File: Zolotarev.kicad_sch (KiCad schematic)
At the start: 176 parts, among them J1 RF_IN, J2 RF_OUT, J3 Conn_02x05_Odd_Even, K1 G5LE-1, K10 G5LE-1, K11 G5LE-1, K12 G5LE-1, K13 G5LE-1, K14 G5LE-1, K2 G5LE-1, K3 G5LE-1, K4 G5LE-1, K5 G5LE-1, K6 G5LE-1, K7 G5LE-1, K8 G5LE-1, K9 G5LE-1

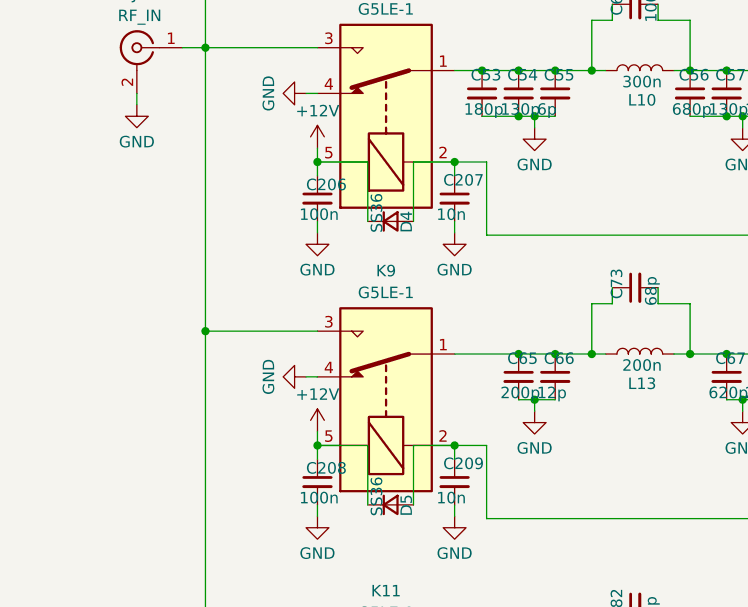
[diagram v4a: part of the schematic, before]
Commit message: 5 bands routed, 2 more to come
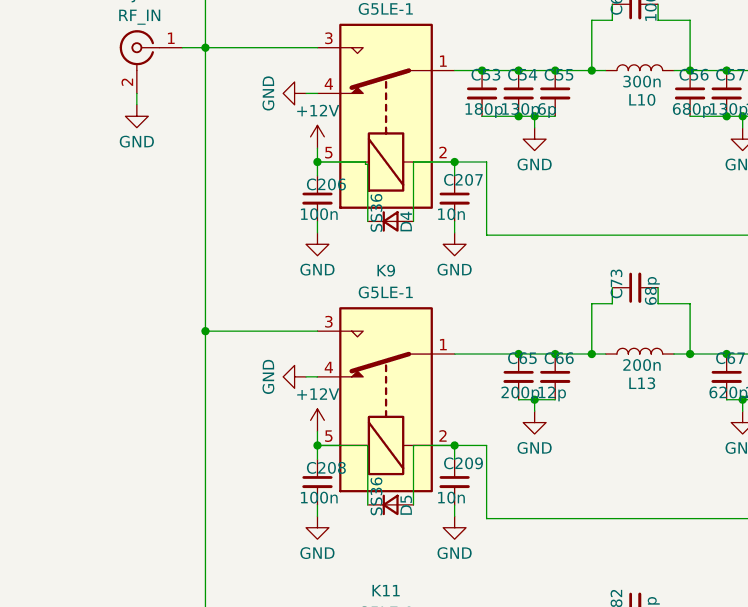
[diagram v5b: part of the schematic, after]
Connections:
- net +12V: now also D4.1 (K), D5.1 (K)
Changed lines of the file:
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@@
 	(wire
 		(pts
-			(xy 46.99 167.64) (xy 41.656 167.64)
+			(xy 46.99 167.64) (xy 41.402 167.64)
 		)
 		(stroke
@@
 	(wire
 		(pts
+			(xy 46.736 136.398) (xy 46.99 136.398)
+		)
+		(stroke
+			(width 0)
+			(type default)
+		)
+	)
+	(wire
+		(pts
 			(xy 110.744 62.992) (xy 112.522 62.992)
 		)
@@
 	(wire
 		(pts
-			(xy 46.99 136.144) (xy 41.656 136.144)
+			(xy 46.736 136.144) (xy 41.402 136.144)
 		)
 		(stroke
@@
 	(wire
 		(pts
-			(xy 46.99 142.748) (xy 46.99 136.144)
+			(xy 46.736 136.398) (xy 46.736 136.144)
 		)
 		(stroke
@@
 		)
 		(stroke
+			(width 0)
+			(type default)
+		)
+	)
+	(wire
+		(pts
+			(xy 46.99 136.398) (xy 46.99 142.748)
+		)
+		(stroke

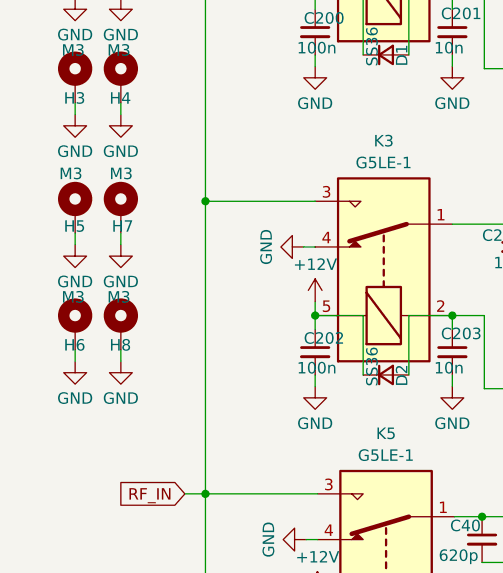
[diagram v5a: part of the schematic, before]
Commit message: all bands routed, command connector to do
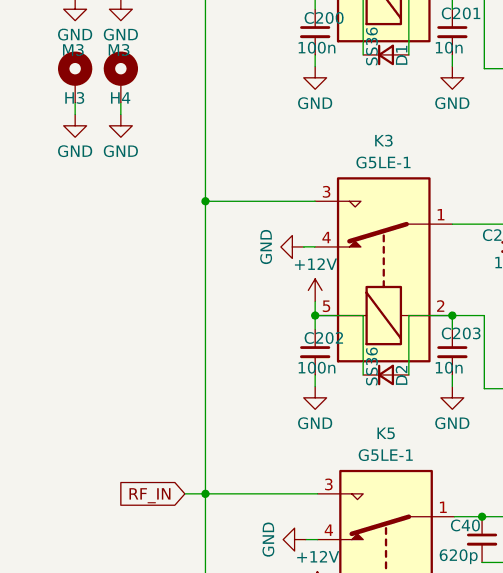
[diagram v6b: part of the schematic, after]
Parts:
- removed H5, H6, H7, H8: M3, MountingHole:MountingHole_3.5mm_Pad_Via, symbol Mechanical:MountingHole_Pad
- D1: footprint Diode_SMD:D_SMC -> Diode_SMD:D_SMB_Handsoldering

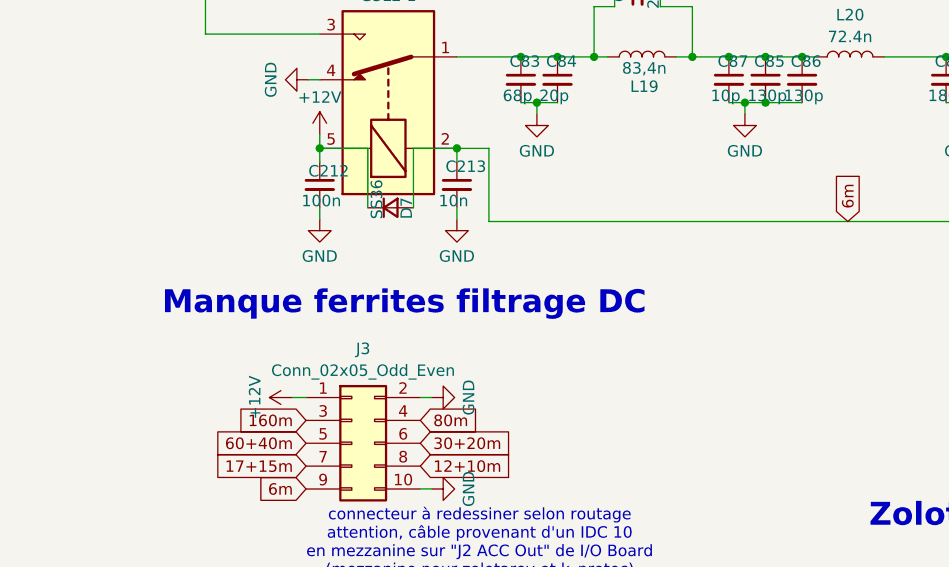
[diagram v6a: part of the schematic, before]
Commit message: silkmask partly added
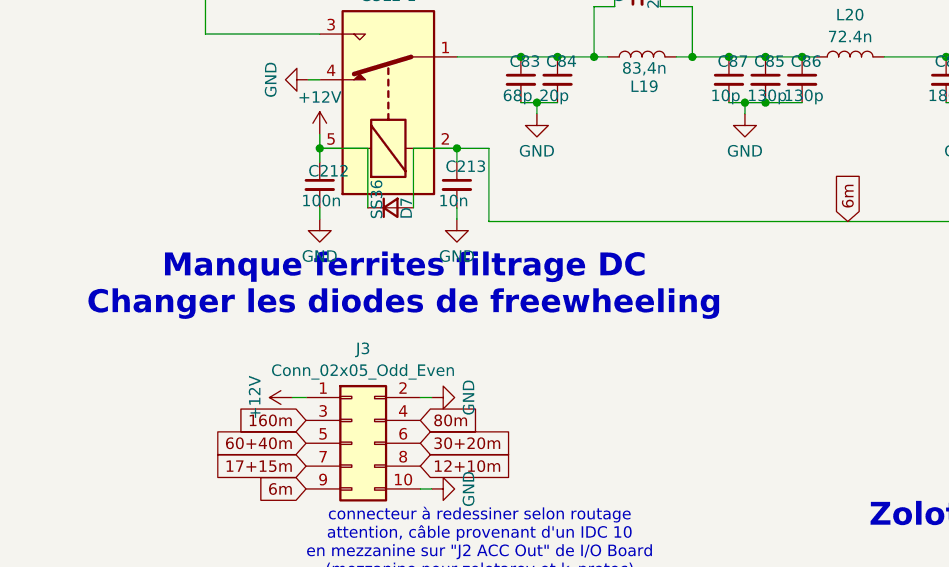
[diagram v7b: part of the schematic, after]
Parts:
- D10, D11, D12, D13, D14, D2, D3, D4, D5, D6, D7, D8, D9: footprint Diode_SMD:D_SMC -> Diode_SMD:D_SMB_Handsoldering
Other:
- note added: "Manque ferrites filtrage DC Changer les diodes de freewheeling"
- note removed: "Manque ferrites filtrage DC"
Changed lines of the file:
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@@
 		)
 	)
-	(text "Manque ferrites filtrage DC\n"
+	(text "Manque ferrites filtrage DC\nChanger les diodes de freewheeling\n\n"
 		(exclude_from_sim no)
 		(at 51.054 252.984 0)
@@
 			)
 		)
-		(property "Footprint" "Diode_SMD:D_SMC"
+		(property "Footprint" "Diode_SMD:D_SMB_Handsoldering"
 			(at 152.146 74.676 90)
 			(effects
@@
 			)
 		)
-		(property "Footprint" "Diode_SMD:D_SMC"
+		(property "Footprint" "Diode_SMD:D_SMB_Handsoldering"
 			(at 49.022 74.676 90)
 			(effects
@@
 			)
 		)
-		(property "Footprint" "Diode_SMD:D_SMC"
+		(property "Footprint" "Diode_SMD:D_SMB_Handsoldering"
 			(at 152.4 142.748 90)
 			(effects
@@
 			)
 		)
-		(property "Footprint" "Diode_SMD:D_SMC"
+		(property "Footprint" "Diode_SMD:D_SMB_Handsoldering"
 			(at 152.4 107.188 90)
 			(effects
@@
 			)
 		)
-		(property "Footprint" "Diode_SMD:D_SMC"
+		(property "Footprint" "Diode_SMD:D_SMB_Handsoldering"
 			(at 49.53 242.316 90)
 			(effects
@@
 			)
 		)
-		(property "Footprint" "Diode_SMD:D_SMC"
+		(property "Footprint" "Diode_SMD:D_SMB_Handsoldering"
 			(at 152.4 174.244 90)
 			(effects
@@
 			)
 		)
-		(property "Footprint" "Diode_SMD:D_SMC"
+		(property "Footprint" "Diode_SMD:D_SMB_Handsoldering"
 			(at 49.276 107.188 90)
 			(effects
@@
 			)
 		)
-		(property "Footprint" "Diode_SMD:D_SMC"
+		(property "Footprint" "Diode_SMD:D_SMB_Handsoldering"
 			(at 152.654 242.316 90)
 			(effects
@@
 			)
 		)
-		(property "Footprint" "Diode_SMD:D_SMC"
+		(property "Footprint" "Diode_SMD:D_SMB_Handsoldering"
 			(at 49.276 209.804 90)
 			(effects
@@
 			)
 		)
-		(property "Footprint" "Diode_SMD:D_SMC"
+		(property "Footprint" "Diode_SMD:D_SMB_Handsoldering"
 			(at 152.4 209.804 90)
 			(effects
@@
 			)
 		)
-		(property "Footprint" "Diode_SMD:D_SMC"
+		(property "Footprint" "Diode_SMD:D_SMB_Handsoldering"
 			(at 49.53 174.244 90)
 			(effects
@@
 			)
 		)
-		(property "Footprint" "Diode_SMD:D_SMC"
+		(property "Footprint" "Diode_SMD:D_SMB_Handsoldering"
 			(at 152.146 39.116 90)
 			(effects
@@
 			)
 		)
-		(property "Footprint" "Diode_SMD:D_SMC"
+		(property "Footprint" "Diode_SMD:D_SMB_Handsoldering"
 			(at 49.53 142.748 90)
 			(effects

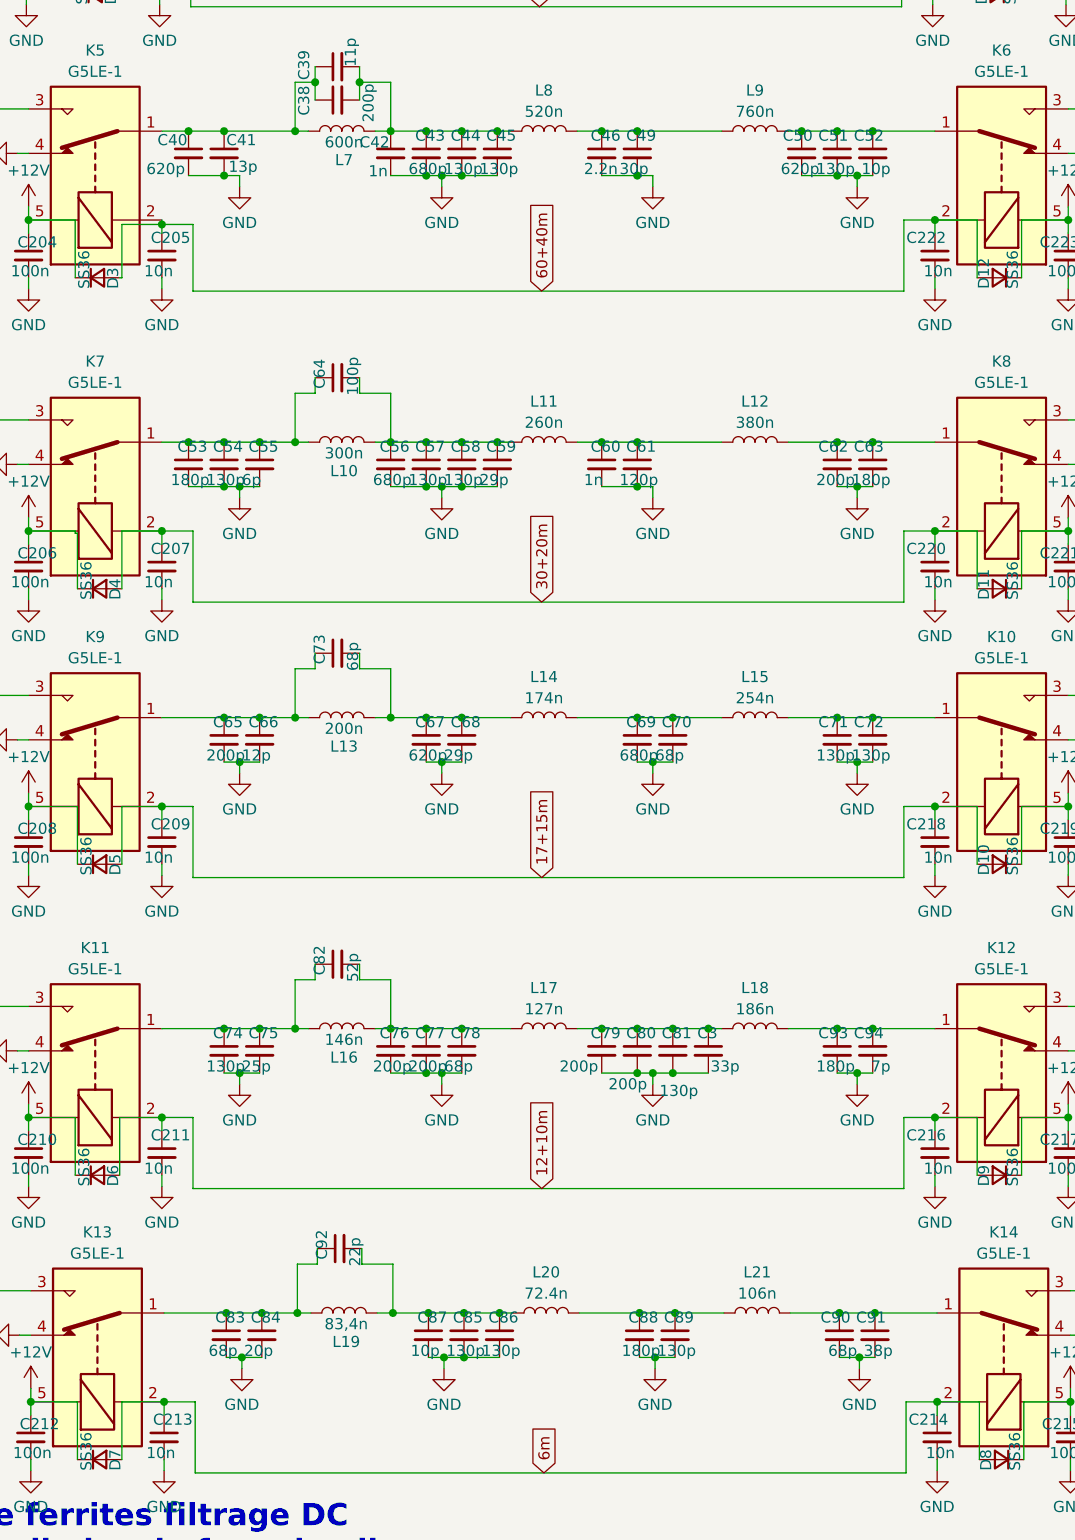
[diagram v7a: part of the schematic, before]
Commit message: diodes changed for smb, silk cleaned
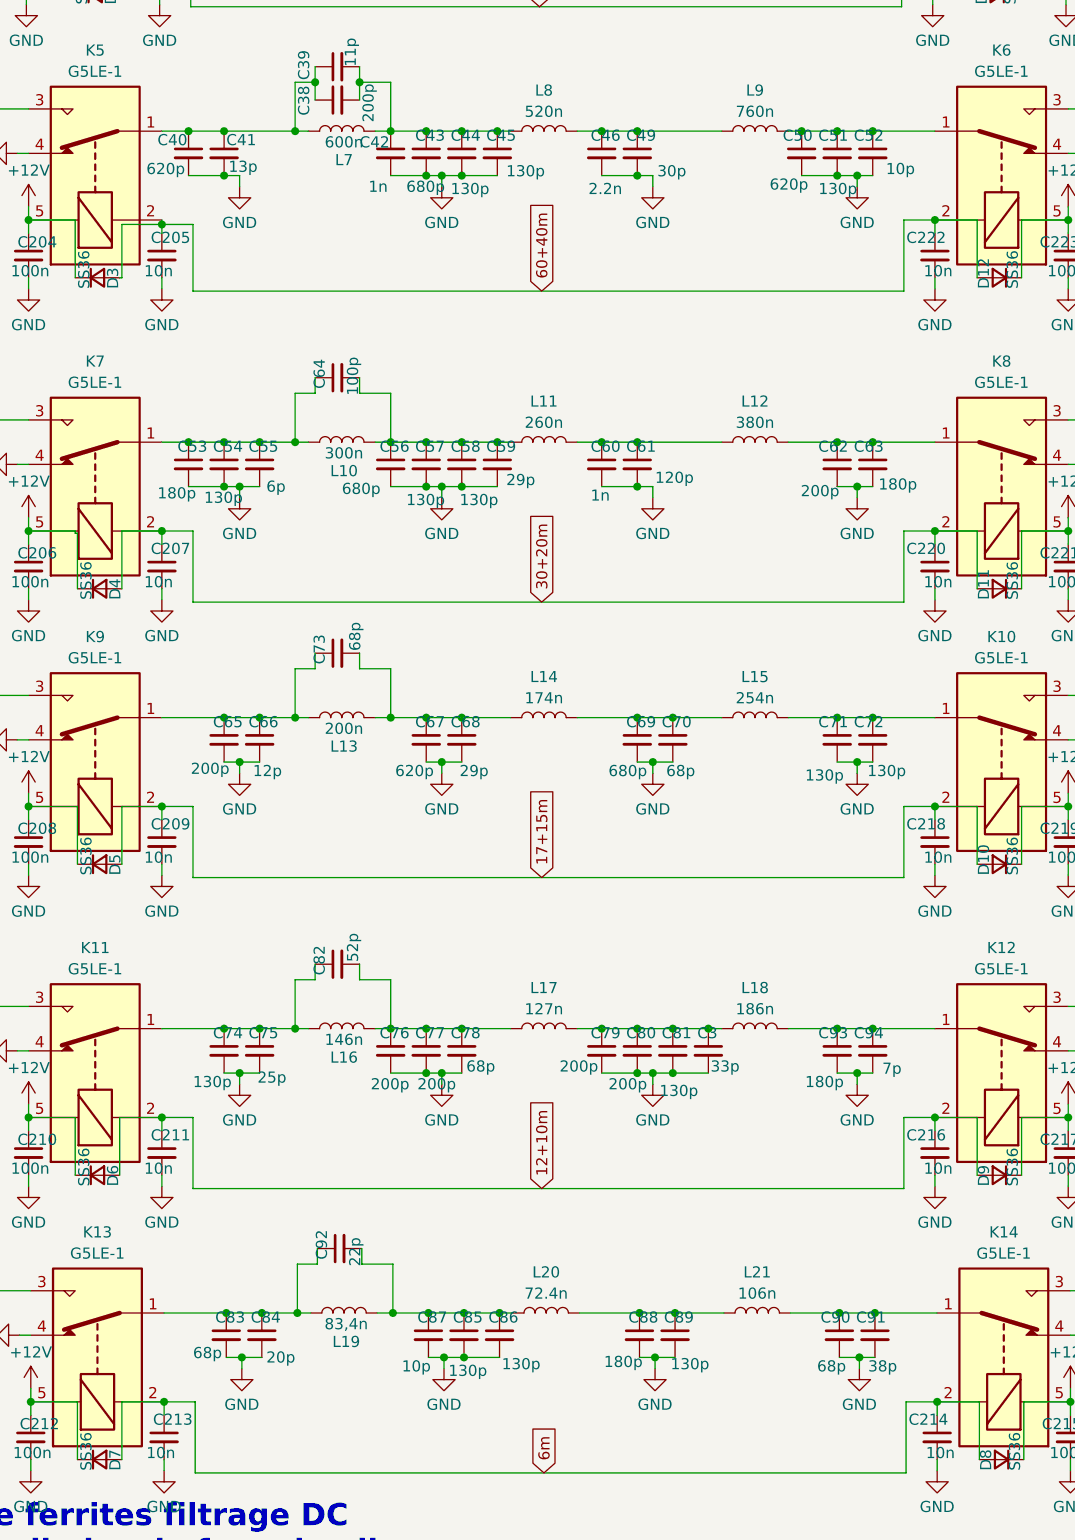
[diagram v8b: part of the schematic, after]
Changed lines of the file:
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@@
 		)
 		(property "Value" "29p"
-			(at 92.964 130.302 0)
+			(at 96.012 130.302 0)
 			(effects
 				(font
@@
 		)
 		(property "Value" "200p"
-			(at 80.772 197.358 0)
+			(at 80.518 199.39 0)
 			(effects
 				(font
@@
 		)
 		(property "Value" "180p"
-			(at 139.954 130.302 0)
+			(at 143.002 130.81 0)
 			(effects
 				(font
@@
 				(font
 					(size 1.27 1.27)
+					(color 255 12 19 1)
 				)
 				(justify left)
@@
 		)
 		(property "Value" "180p"
-			(at 57.658 130.302 0)
+			(at 56.134 131.826 0)
 			(effects
 				(font
@@
 		)
 		(property "Value" "20p"
-			(at 66.04 229.87 0)
+			(at 68.58 230.632 0)
 			(effects
 				(font
@@
 				(font
 					(size 1.27 1.27)
+					(color 255 8 37 1)
 				)
 				(justify left)
@@
 		)
 		(property "Value" "130p"
-			(at 88.9 94.742 0)
+			(at 89.662 97.028 0)
 			(effects
 				(font
@@
 		)
 		(property "Value" "130p"
-			(at 61.722 197.358 0)
+			(at 60.198 199.136 0)
 			(effects
 				(font
@@
 				(font
 					(size 1.27 1.27)
+					(color 255 8 37 1)
 				)
 				(justify left)
@@
 		)
 		(property "Value" "130p"
-			(at 61.722 130.302 0)
+			(at 61.468 132.334 0)
 			(effects
 				(font
@@
 		)
 		(property "Value" "7p"
-			(at 139.954 197.358 0)
+			(at 141.224 197.612 0)
 			(effects
 				(font
@@
 		)
 		(property "Value" "620p"
-			(at 131.826 94.742 0)
+			(at 130.556 96.52 0)
 			(effects
 				(font
 					(size 1.27 1.27)
+					(color 255 8 37 1)
 				)
 				(justify left)
@@
 		)
 		(property "Value" "680p"
-			(at 80.772 130.302 0)
+			(at 77.216 131.318 0)
 			(effects
 				(font
 					(size 1.27 1.27)
+					(color 255 8 37 1)
 				)
 				(justify left)
@@
 				(font
 					(size 1.27 1.27)
+					(color 255 8 37 1)
 				)
 				(justify left)
@@
 		)
 		(property "Value" "130p"
-			(at 93.218 229.87 0)
+			(at 95.504 231.394 0)
 			(effects
 				(font
@@
 		)
 		(property "Value" "130p"
-			(at 92.964 94.742 0)
+			(at 96.012 94.996 0)
 			(effects
 				(font
@@
 				(font
 					(size 1.27 1.27)
+					(color 255 8 37 1)
 				)
 				(justify left)
@@
 		)
 		(property "Value" "200p"
-			(at 61.722 161.798 0)
+			(at 59.944 163.322 0)
 			(effects
 				(font
@@
 		)
 		(property "Value" "2.2n"
-			(at 104.902 94.742 0)
+			(at 105.41 97.028 0)
 			(effects
 				(font
 					(size 1.27 1.27)
+					(color 255 8 37 1)
 				)
 				(justify left)
@@
 		)
 		(property "Value" "130p"
-			(at 84.836 130.302 0)
+			(at 84.582 132.588 0)
 			(effects
 				(font
@@
 		)
 		(property "Value" "130p"
-			(at 139.954 161.798 0)
+			(at 141.732 163.576 0)
 			(effects
 				(font
@@
 		)
 		(property "Value" "10p"
-			(at 139.954 94.742 0)
+			(at 142.748 94.742 0)
 			(effects
 				(font
@@
 				(font
 					(size 1.27 1.27)
+					(color 255 8 37 1)
 				)
 				(justify left)
@@
 		)
 		(property "Value" "680p"
-			(at 108.966 161.798 0)
+			(at 107.696 163.576 0)
 			(effects
 				(font
 					(size 1.27 1.27)
+					(color 255 8 37 1)
 				)
 				(justify left)
@@
 				(font
 					(size 1.27 1.27)
+					(color 255 16 20 1)
 				)
 				(justify left)
@@
 				(font
 					(size 1.27 1.27)
+					(color 255 8 37 1)
 				)
 				(justify left)
@@
 		)
 		(property "Value" "180p"
-			(at 135.89 197.358 0)
+			(at 134.62 199.136 0)
 			(effects
 				(font
@@
 		)
 		(property "Value" "620p"
-			(at 84.836 161.798 0)
+			(at 83.312 163.576 0)
 			(effects
 				(font
@@
 		)
 		(property "Value" "130p"
-			(at 89.154 229.87 0)
+			(at 89.408 232.156 0)
 			(effects
 				(font
@@
 		)
 		(property "Value" "68p"
-			(at 113.03 161.798 0)
+			(at 114.3 163.576 0)
 			(effects
 				(font
@@
 		)
 		(property "Value" "200p"
-			(at 84.836 197.358 0)
+			(at 85.852 199.39 0)
 			(effects
 				(font
@@
 		)
 		(property "Value" "68p"
-			(at 136.144 229.87 0)
+			(at 134.874 231.648 0)
 			(effects
 				(font
@@
 		)
 		(property "Value" "38p"
-			(at 140.208 229.87 0)
+			(at 140.716 231.648 0)
 			(effects
 				(font
@@
 		)
 		(property "Value" "200p"
-			(at 135.89 130.302 0)
+			(at 134.112 131.572 0)
 			(effects
 				(font
@@
 		)
 		(property "Value" "130p"
-			(at 135.89 94.742 0)
+			(at 136.144 97.028 0)
 			(effects
 				(font
@@
 				(font
 					(size 1.27 1.27)
+					(color 255 8 37 1)
 				)
 				(justify left)
@@
 		)
 		(property "Value" "68p"
-			(at 78.486 152.146 0)
+			(at 78.74 149.86 0)
 			(effects
 				(font
@@
 		)
 		(property "Value" "68p"
-			(at 88.9 197.358 0)
+			(at 91.44 197.358 0)
 			(effects
 				(font
@@
 		)
 		(property "Value" "680p"
-			(at 84.836 94.742 0)
+			(at 84.582 96.774 0)
 			(effects
 				(font
 					(size 1.27 1.27)
+					(color 255 8 37 1)
 				)
 				(justify left)
@@
 		)
 		(property "Value" "180p"
-			(at 109.22 229.87 0)
+			(at 107.188 231.14 0)
 			(effects
 				(font
@@
 		)
 		(property "Value" "1n"
-			(at 104.902 130.302 0)
+			(at 105.664 132.08 0)
 			(effects
 				(font
 					(size 1.27 1.27)
+					(color 255 8 37 1)
 				)
 				(justify left)
@@
 		)
 		(property "Value" "6p"
-			(at 65.786 130.302 0)
+			(at 68.58 131.064 0)
 			(effects
 				(font
@@
 		)
 		(property "Value" "25p"
-			(at 65.786 197.358 0)
+			(at 67.564 198.628 0)
 			(effects
 				(font
@@
 		)
 		(property "Value" "130p"
-			(at 135.89 161.798 0)
+			(at 134.62 164.084 0)
 			(effects
 				(font
@@
 		)
 		(property "Value" "1n"
-			(at 80.264 94.996 0)
+			(at 80.264 96.774 0)
 			(effects
 				(font
 					(size 1.27 1.27)
+					(color 255 8 37 1)
 				)
 				(justify left)
@@
 				(font
 					(size 1.27 1.27)
+					(color 255 8 37 1)
 				)
 				(justify left)
@@
 		)
 		(property "Value" "68p"
-			(at 61.976 229.87 0)
+			(at 60.198 230.124 0)
 			(effects
 				(font
@@
 				(font
 					(size 1.27 1.27)
+					(color 255 8 37 1)
 				)
 				(justify left)
@@
 		)
 		(property "Value" "29p"
-			(at 88.9 161.798 0)
+			(at 90.678 163.576 0)
 			(effects
 				(font
@@
 		)
 		(property "Value" "52p"
-			(at 78.486 187.706 0)
+			(at 78.486 185.42 0)
 			(effects
 				(font
@@
 		)
 		(property "Value" "10p"
-			(at 85.09 229.87 0)
+			(at 84.074 231.648 0)
 			(effects
 				(font
@@
 		)
 		(property "Value" "130p"
-			(at 113.284 229.87 0)
+			(at 114.808 231.394 0)
 			(effects
 				(font
@@
 				(font
 					(size 1.27 1.27)
+					(color 255 15 51 1)
 				)
 				(justify left)
@@
 		)
 		(property "Value" "12p"
-			(at 65.786 161.798 0)
+			(at 67.056 163.576 0)
 			(effects
 				(font
@@
 		)
 		(property "Value" "130p"
-			(at 88.9 130.302 0)
+			(at 90.678 132.588 0)
 			(effects
 				(font
@@
 		)
 		(property "Value" "120p"
-			(at 108.966 130.302 0)
+			(at 113.03 130.048 0)
 			(effects
 				(font
@@
 		)
 		(property "Value" "30p"
-			(at 108.966 94.742 0)
+			(at 113.284 94.996 0)
 			(effects
 				(font
